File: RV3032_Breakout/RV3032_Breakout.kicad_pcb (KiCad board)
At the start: 2 copper layers, 14.1 x 13.8 mm, 11 parts, among them J2 Conn_01x05_Female

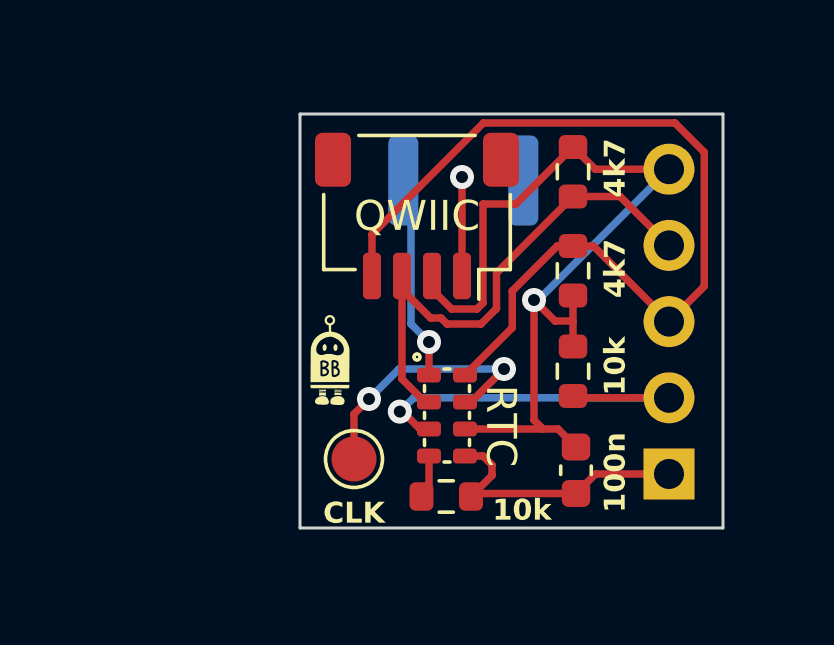
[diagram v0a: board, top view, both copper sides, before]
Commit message: Updated to use supercap instead of battery
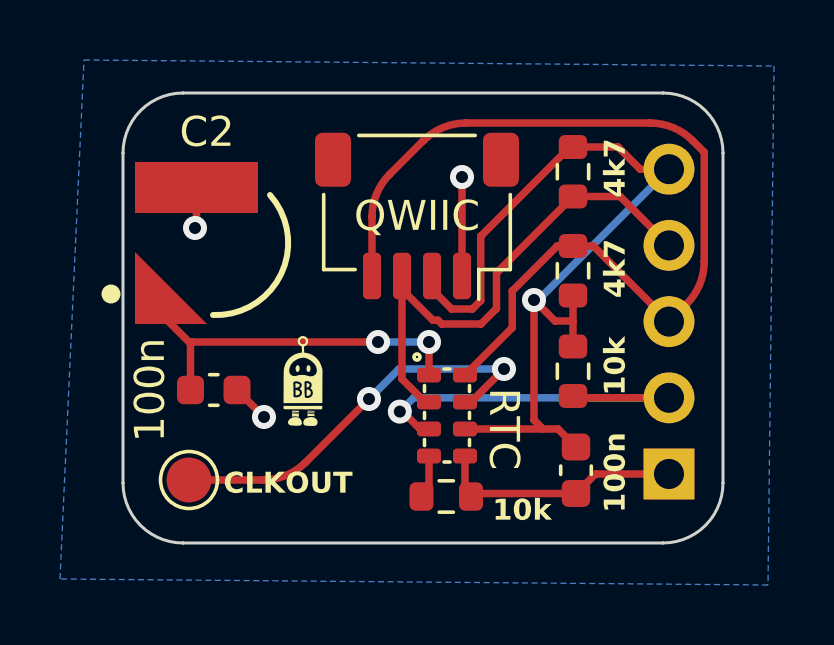
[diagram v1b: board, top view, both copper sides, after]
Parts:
- removed BT1: 3.0, Battery:CR44_Tabs
- added 100n: 100n, Capacitor_SMD:C_0603_1608Metric, F.Cu at (125.0, 99.9)
- added C2: XH414HG-IV01E, Larry:CAP_XH414HG-IV01E, F.Cu at (125.1, 95.0)
- moved CLKOUT 5.54 mm to (124.2, 102.9)
- moved G*** 1.14 mm to (128.0, 99.6)
- renumbered CLK to CLKOUT
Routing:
- net Net-(RTC1-VBACKUP): track 6.35 -> 12.4 mm, vias 1 -> 2
- net Net-(RTC1-CLKOUT): track 8.88 -> 13.7 mm
- net GND: track 12.6 -> 14.3 mm, vias 1 -> 3
- net +3.3V: track 30.6 -> 29.9 mm
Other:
- board size 14.1 x 13.8 mm -> 20 x 15 mm
- board text added: "RV3032C7 Breakout with SuperCapacitor Backup Power"
- board text removed: "CR44 3.0V"
- board text removed: "RV3032C7 Breakout"
